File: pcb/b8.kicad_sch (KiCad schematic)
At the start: 29 parts, among them J1 USB, J2 ISP Programming, SW1 SW_Push, SW2 SW_Push, SW3 SW_Push, SW4 SW_Push, SW5 SW_Push, SW6 SW_Push, SW7 SW_Push, SW8 SW_Push, U1 ATtiny2313A-P, Y1 20MHz

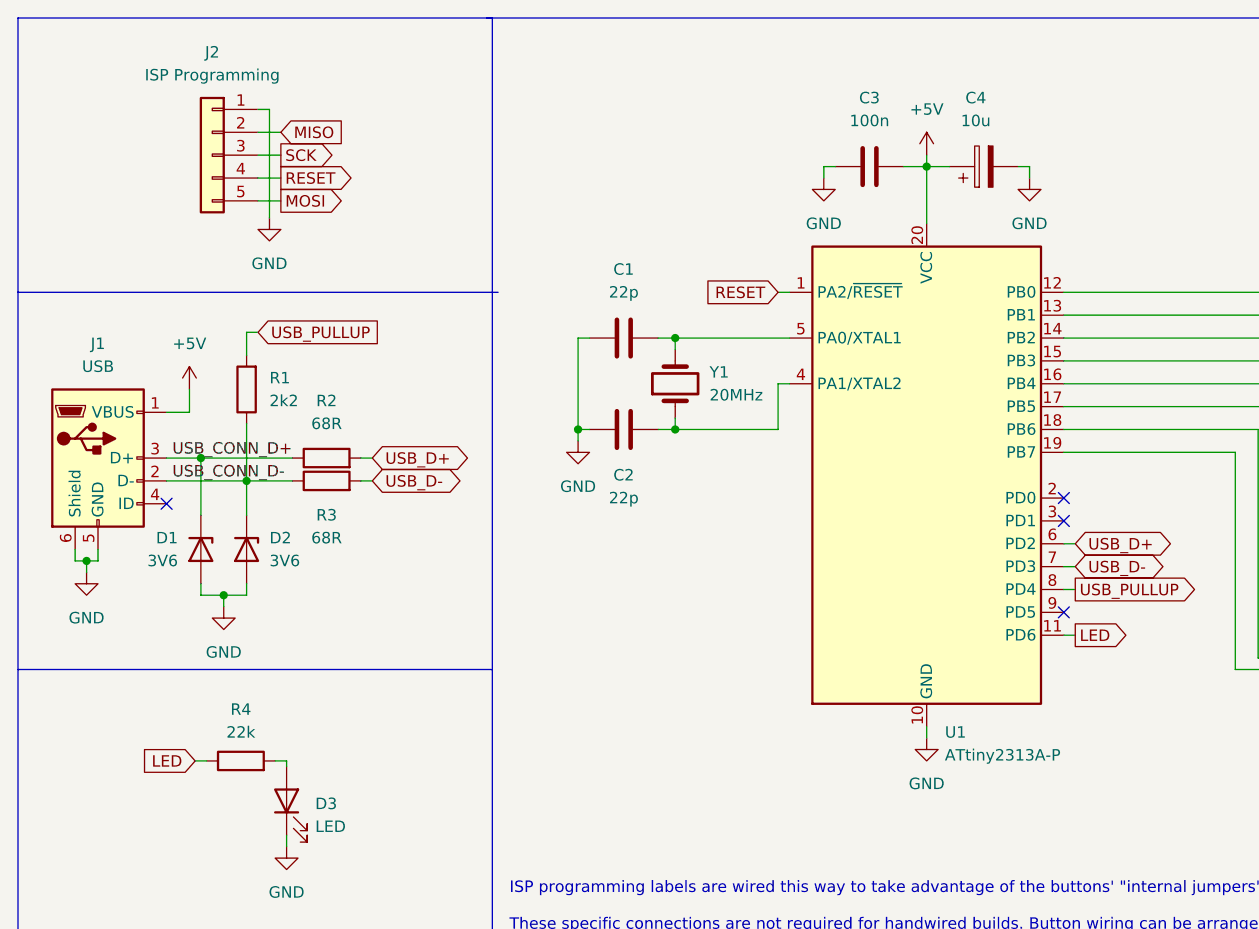
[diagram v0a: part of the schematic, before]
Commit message: pcb: revision 1.1
this revision adds a 6th pin to ISP programming header, to allow usage
of official Microchip probes, like PICKit 4. It also fixes alignment and
dimensions of the buttons.
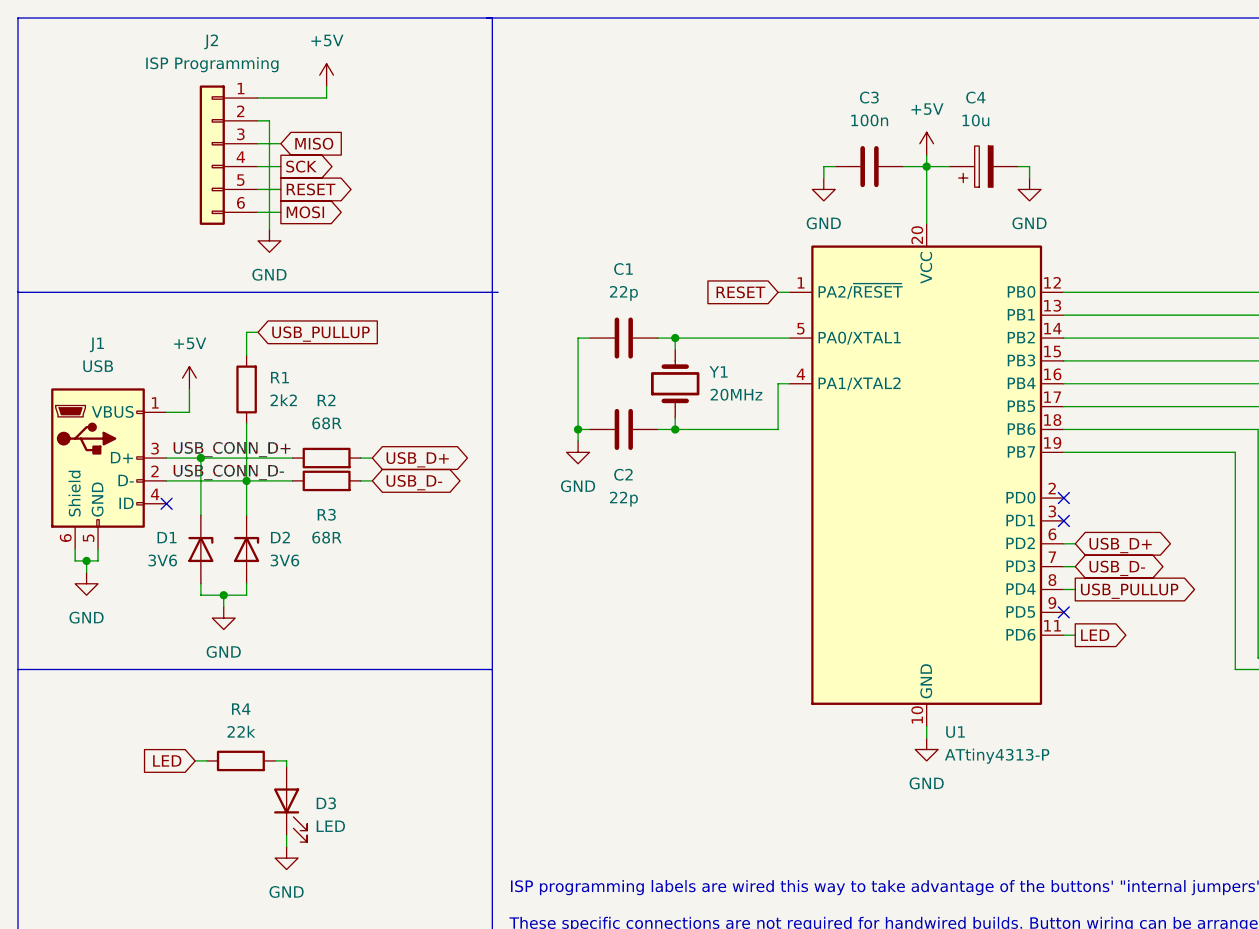
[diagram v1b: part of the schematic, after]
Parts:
- J2: footprint Connector_PinHeader_2.54mm:PinHeader_1x05_P2.54mm_Horizontal -> Connector_PinHeader_2.54mm:PinHeader_1x06_P2.54mm_Horizontal; symbol Connector_Generic:Conn_01x05 -> Connector_Generic:Conn_01x06
- U1: value ATtiny2313A-P -> ATtiny4313-P; symbol MCU_Microchip_ATtiny:ATtiny2313A-P -> MCU_Microchip_ATtiny:ATtiny4313-P
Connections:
- net +5V: now also J2.1 (Pin_1)
- net GND: now also J2.2 (Pin_2); no longer J2.1 (Pin_1)
- net MISO: now also J2.3 (Pin_3); no longer J2.2 (Pin_2)
- net MOSI: now also J2.6 (Pin_6); no longer J2.5 (Pin_5)
- net RESET: now also J2.5 (Pin_5); no longer J2.4 (Pin_4)
- net SCK: now also J2.4 (Pin_4); no longer J2.3 (Pin_3)
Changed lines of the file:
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@@
   (title_block
     (title "b8")
-    (date "2022-10-21")
-    (rev "1.0")
+    (date "2022-12-22")
+    (rev "1.1")
     (comment 3 "Released under CERN Open Hardware Licence Version 2 - Strongly Reciprocal")
     (comment 4 "Designed by: Rafael G. Martins")
@@
     (stroke (width 0) (type default) (color 0 0 0 0))
   )
-  (wire (pts (xy 80.01 56.515) (xy 82.55 56.515))
-    (stroke (width 0) (type default) (color 0 0 0 0))
-  )
   (wire (pts (xy 165.735 61.595) (xy 165.735 60.325))
     (stroke (width 0) (type default) (color 0 0 0 0))
@@
     (stroke (width 0) (type default) (color 0 0 0 0))
   )
-  (wire (pts (xy 81.28 53.975) (xy 81.28 66.04))
+  (wire (pts (xy 81.28 55.245) (xy 81.28 67.31))
     (stroke (width 0) (type default) (color 0 0 0 0))
   )
@@
     (stroke (width 0) (type default) (color 0 0 0 0))
   )
+  (wire (pts (xy 80.01 52.705) (xy 87.63 52.705))
+    (stroke (width 0) (type default) (color 0 0 0 0))
+  )
   (wire (pts (xy 230.505 112.395) (xy 231.775 112.395))
     (stroke (width 0) (type default) (color 0 0 0 0))
@@
     (stroke (width 0) (type default) (color 0 0 0 0))
   )
+  (wire (pts (xy 80.01 57.785) (xy 82.55 57.785))
+    (stroke (width 0) (type default) (color 0 0 0 0))
+  )
   (wire (pts (xy 165.735 60.325) (xy 164.465 60.325))
     (stroke (width 0) (type default) (color 0 0 0 0))
@@
     (stroke (width 0) (type default) (color 0 0 0 0))
   )
-  (wire (pts (xy 80.01 59.055) (xy 82.55 59.055))
-    (stroke (width 0) (type default) (color 0 0 0 0))
-  )
   (wire (pts (xy 231.775 114.935) (xy 231.775 112.395))
     (stroke (width 0) (type default) (color 0 0 0 0))
@@
     (stroke (width 0) (type default) (color 0 0 0 0))
   )
+  (wire (pts (xy 87.63 52.705) (xy 87.63 51.435))
+    (stroke (width 0) (type default) (color 0 0 0 0))
+  )
   (wire (pts (xy 169.545 104.775) (xy 170.815 104.775))
     (stroke (width 0) (type default) (color 0 0 0 0))
@@
     (stroke (width 0) (type default) (color 0 0 0 0))
   )
+  (wire (pts (xy 80.01 62.865) (xy 82.55 62.865))
+    (stroke (width 0) (type default) (color 0 0 0 0))
+  )
   (wire (pts (xy 115.57 89.535) (xy 115.57 79.375))
     (stroke (width 0) (type default) (color 0 0 0 0))
@@
     (stroke (width 0) (type default) (color 0 0 0 0))
   )
-  (wire (pts (xy 80.01 53.975) (xy 81.28 53.975))
+  (wire (pts (xy 80.01 65.405) (xy 82.55 65.405))
     (stroke (width 0) (type default) (color 0 0 0 0))
   )
@@
     (stroke (width 0) (type default) (color 0 0 0 0))
   )
-  (wire (pts (xy 80.01 64.135) (xy 82.55 64.135))
-    (stroke (width 0) (type default) (color 0 0 0 0))
-  )
   (wire (pts (xy 216.535 75.565) (xy 216.535 74.295))
     (stroke (width 0) (type default) (color 0 0 0 0))
@@
     (stroke (width 0) (type default) (color 0 0 0 0))
   )
+  (wire (pts (xy 80.01 55.245) (xy 81.28 55.245))
+    (stroke (width 0) (type default) (color 0 0 0 0))
+  )
+  (wire (pts (xy 80.01 60.325) (xy 82.55 60.325))
+    (stroke (width 0) (type default) (color 0 0 0 0))
+  )
   (wire (pts (xy 230.505 74.295) (xy 231.775 74.295))
     (stroke (width 0) (type default) (color 0 0 0 0))
@@
   )
   (wire (pts (xy 201.295 79.375) (xy 201.295 85.09))
-    (stroke (width 0) (type default) (color 0 0 0 0))
-  )
-  (wire (pts (xy 80.01 61.595) (xy 82.55 61.595))
     (stroke (width 0) (type default) (color 0 0 0 0))
   )
@@
     )
   )
-  (global_label "MISO" (shape input) (at 82.55 56.515 0) (fields_autoplaced)
+  (global_label "MISO" (shape input) (at 82.55 57.785 0) (fields_autoplaced)
     (effects (font (size 1.27 1.27)) (justify left))
-    (property "Intersheet References" "${INTERSHEET_REFS}" (id 0) (at 89.5593 56.4356 0)
+    (property "Intersheet References" "${INTERSHEET_REFS}" (id 0) (at 89.5593 57.7056 0)
       (effects (font (size 1.27 1.27)) (justify left) hide)
     )
   )
-  (global_label "RESET" (shape output) (at 82.55 61.595 0) (fields_autoplaced)
+  (global_label "RESET" (shape output) (at 82.55 62.865 0) (fields_autoplaced)
     (effects (font (size 1.27 1.27)) (justify left))
-    (property "Intersheet References" "${INTERSHEET_REFS}" (id 0) (at 90.7083 61.5156 0)
+    (property "Intersheet References" "${INTERSHEET_REFS}" (id 0) (at 90.7083 62.7856 0)
       (effects (font (size 1.27 1.27)) (justify left) hide)
     )
@@
     )
   )
-  (global_label "MOSI" (shape output) (at 82.55 64.135 0) (fields_autoplaced)
+  (global_label "MOSI" (shape output) (at 82.55 65.405 0) (fields_autoplaced)
     (effects (font (size 1.27 1.27)) (justify left))
-    (property "Intersheet References" "${INTERSHEET_REFS}" (id 0) (at 89.5593 64.0556 0)
+    (property "Intersheet References" "${INTERSHEET_REFS}" (id 0) (at 89.5593 65.3256 0)
       (effects (font (size 1.27 1.27)) (justify left) hide)
     )
   )
-  (global_label "SCK" (shape output) (at 82.55 59.055 0) (fields_autoplaced)
+  (global_label "SCK" (shape output) (at 82.55 60.325 0) (fields_autoplaced)
     (effects (font (size 1.27 1.27)) (justify left))
-    (property "Intersheet References" "${INTERSHEET_REFS}" (id 0) (at 88.7126 58.9756 0)
+    (property "Intersheet References" "${INTERSHEET_REFS}" (id 0) (at 88.7126 60.2456 0)
       (effects (font (size 1.27 1.27)) (justify left) hide)
     )
@@
     (pin "1")
   )
-  (symbol (lib_id "MCU_Microchip_ATtiny:ATtiny2313A-P") (at 154.305 94.615 0) (unit 1)
+  (symbol (lib_id "MCU_Microchip_ATtiny:ATtiny4313-P") (at 154.305 94.615 0) (unit 1)
     (in_bom yes) (on_board yes) (fields_autoplaced)
     (property "Reference" "U1" (id 0) (at 156.3244 123.19 0)
       (effects (font (size 1.27 1.27)) (justify left))
     )
-    (property "Value" "ATtiny2313A-P" (id 1) (at 156.3244 125.73 0)
+    (property "Value" "ATtiny4313-P" (id 1) (at 156.3244 125.73 0)
       (effects (font (size 1.27 1.27)) (justify left))
     )
@@
     (pin "1")
   )
-  (symbol (lib_id "Connector_Generic:Conn_01x05") (at 74.93 59.055 0) (mirror y) (unit 1)
-    (in_bom yes) (on_board yes) (fields_autoplaced)
-    (property "Reference" "J2" (id 0) (at 74.93 47.625 0))
-    (property "Value" "ISP Programming" (id 1) (at 74.93 50.165 0))
-    (property "Footprint" "Connector_PinHeader_2.54mm:PinHeader_1x05_P2.54mm_Horizontal" (id 2) (at 74.93 59.055 0)
-      (effects (font (size 1.27 1.27)) hide)
-    )
-    (property "Datasheet" "~" (id 3) (at 74.93 59.055 0)
+  (symbol (lib_id "Connector_Generic:Conn_01x06") (at 74.93 57.785 0) (mirror y) (unit 1)
+    (in_bom yes) (on_board yes) (fields_autoplaced)
+    (property "Reference" "J2" (id 0) (at 74.93 46.355 0))
+    (property "Value" "ISP Programming" (id 1) (at 74.93 48.895 0))
+    (property "Footprint" "Connector_PinHeader_2.54mm:PinHeader_1x06_P2.54mm_Horizontal" (id 2) (at 74.93 57.785 0)
+      (effects (font (size 1.27 1.27)) hide)
+    )
+    (property "Datasheet" "~" (id 3) (at 74.93 57.785 0)
       (effects (font (size 1.27 1.27)) hide)
     )
@@
     (pin "4")
     (pin "5")
+    (pin "6")
   )
   (symbol (lib_id "power:+5V") (at 154.305 59.055 0) (unit 1)
@@
     (pin "1")
   )
+  (symbol (lib_id "power:+5V") (at 87.63 51.435 0) (unit 1)
+    (in_bom yes) (on_board yes) (fields_autoplaced)
+    (property "Reference" "#PWR0114" (id 0) (at 87.63 55.245 0)
+      (effects (font (size 1.27 1.27)) hide)
+    )
+    (property "Value" "+5V" (id 1) (at 87.63 46.355 0))
+    (property "Footprint" "" (id 2) (at 87.63 51.435 0)
+      (effects (font (size 1.27 1.27)) hide)
+    )
+    (property "Datasheet" "" (id 3) (at 87.63 51.435 0)
+      (effects (font (size 1.27 1.27)) hide)
+    )
+    (pin "1")
+  )
   (symbol (lib_id "custom:SW_Push") (at 207.645 98.425 0) (unit 1)
     (in_bom yes) (on_board yes) (fields_autoplaced)
@@
     (pin "2")
   )
-  (symbol (lib_id "power:GND") (at 81.28 66.04 0) (unit 1)
-    (in_bom yes) (on_board yes) (fields_autoplaced)
-    (property "Reference" "#PWR0103" (id 0) (at 81.28 72.39 0)
-      (effects (font (size 1.27 1.27)) hide)
-    )
-    (property "Value" "GND" (id 1) (at 81.28 71.12 0))
-    (property "Footprint" "" (id 2) (at 81.28 66.04 0)
-      (effects (font (size 1.27 1.27)) hide)
-    )
-    (property "Datasheet" "" (id 3) (at 81.28 66.04 0)
+  (symbol (lib_id "power:GND") (at 81.28 67.31 0) (unit 1)
+    (in_bom yes) (on_board yes) (fields_autoplaced)
+    (property "Reference" "#PWR0103" (id 0) (at 81.28 73.66 0)
+      (effects (font (size 1.27 1.27)) hide)
+    )
+    (property "Value" "GND" (id 1) (at 81.28 72.39 0))
+    (property "Footprint" "" (id 2) (at 81.28 67.31 0)
+      (effects (font (size 1.27 1.27)) hide)
+    )
+    (property "Datasheet" "" (id 3) (at 81.28 67.31 0)
       (effects (font (size 1.27 1.27)) hide)
     )
@@
       (reference "#PWR0113") (unit 1) (value "GND") (footprint "")
     )
+    (path "/bf108bb0-8689-4bd2-a66b-9f206e4becb9"
+      (reference "#PWR0114") (unit 1) (value "+5V") (footprint "")
+    )
     (path "/365ebf4f-be31-4672-aafd-106b8f76df91"
       (reference "C1") (unit 1) (value "22p") (footprint "Capacitor_THT:C_Disc_D3.0mm_W1.6mm_P2.50mm")
@@
     )
     (path "/adc69150-9fe5-434c-b0e0-7922e0d28d4a"
-      (reference "J2") (unit 1) (value "ISP Programming") (footprint "Connector_PinHeader_2.54mm:PinHeader_1x05_P2.54mm_Horizontal")
+      (reference "J2") (unit 1) (value "ISP Programming") (footprint "Connector_PinHeader_2.54mm:PinHeader_1x06_P2.54mm_Horizontal")
     )
     (path "/dd51b2c6-2e06-43ad-807b-7b1e535c7a84"
@@
     )
     (path "/1095e697-354a-4df5-bed0-f205c492dce5"
-      (reference "U1") (unit 1) (value "ATtiny2313A-P") (footprint "Package_DIP:DIP-20_W7.62mm")
+      (reference "U1") (unit 1) (value "ATtiny4313-P") (footprint "Package_DIP:DIP-20_W7.62mm")
     )
     (path "/ec71272c-37d2-4107-9034-c9a8edf92e00"
